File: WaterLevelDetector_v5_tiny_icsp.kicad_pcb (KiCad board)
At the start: 2 copper layers, 57 x 90 mm, 12 parts, among them J3 USB_C_Receptacle_PowerOnly_6P, J4 Conn_02x03_Odd_Even, U1 ATtiny85-20P

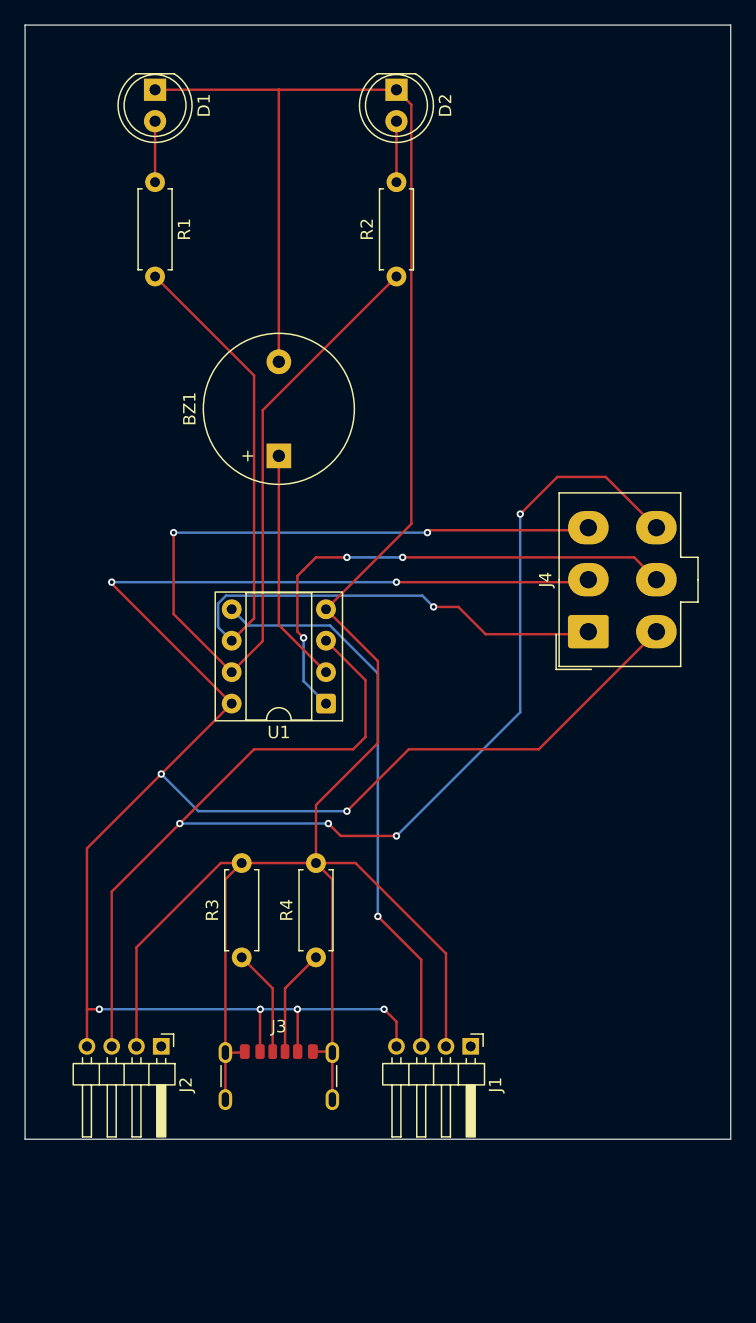
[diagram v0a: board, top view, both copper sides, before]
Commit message: made the pcb area smaller
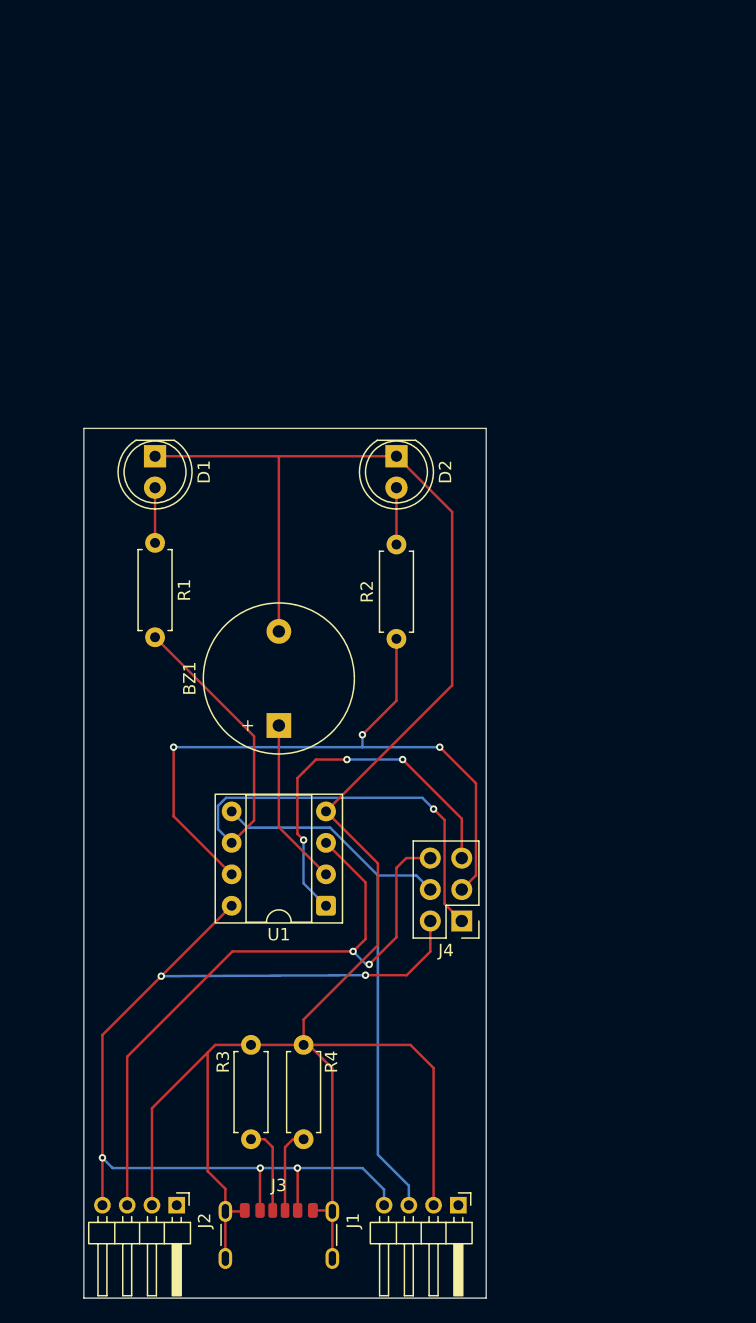
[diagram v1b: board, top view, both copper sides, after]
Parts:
- J4: footprint Connector_Molex:Molex_Mini-Fit_Jr_5566-06A_2x03_P4.20mm_Vertical -> Connector_PinHeader_2.54mm:PinHeader_2x03_P2.54mm_Vertical
- moved D1 29.6 mm to (136.0, 71.3)
- moved D2 29.6 mm to (155.5, 71.3)
- moved R2 29.3 mm to (155.5, 86.1)
- moved R1 29.1 mm to (136.0, 78.3)
- moved J4 25.5 mm to (160.8, 108.9), turned to 180 degrees
- moved BZ1 21.8 mm to (146.0, 93.1)
- moved U1 16.3 mm to (149.8, 107.6)
- moved R4 14.7 mm to (148.0, 126.5)
- moved R3 14.7 mm to (143.8, 126.5)
- moved J2 12.9 mm to (137.8, 131.8)
- moved J1 12.9 mm to (160.5, 131.8)
- moved J3 12.8 mm to (146.0, 135.3)
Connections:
- J4 pad 4: Net-(J1-Pin_4) -> Net-(J1-Pin_3)
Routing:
- net Net-(J1-Pin_4): track 166.5 -> 85.4 mm, vias 8 -> 5
- net Net-(J2-Pin_3): track 109.3 -> 57.9 mm, vias 4 -> 2
- net Net-(J4-Pin_3): track 84.4 -> 56.8 mm, vias 2 -> 3
- net Net-(BZ1--): track 200.0 -> 176.0 mm
- net Net-(J4-Pin_1): track 68.5 -> 52.2 mm
- net Net-(J4-Pin_5): track 41.6 -> 30.3 mm
- net Net-(BZ1-+): track 19.0 -> 13.6 mm
- net Net-(J3-CC2): track 8.65 -> 6.88 mm
- net Net-(J3-CC1): track 8.65 -> 7.13 mm
- net Net-(J1-Pin_3): track 45.5 -> 46.3 mm, vias 1 -> 0
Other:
- board size 57 x 90 mm -> 32.5 x 70.3 mm

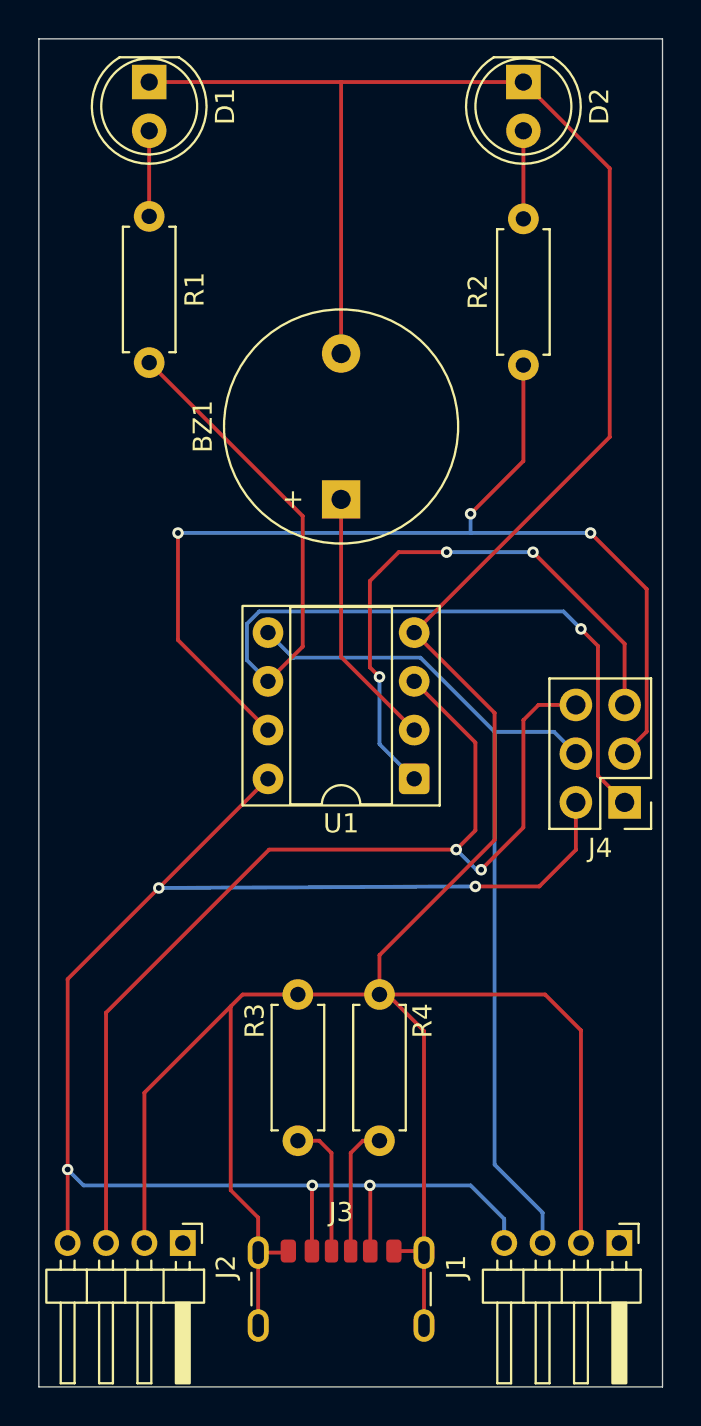
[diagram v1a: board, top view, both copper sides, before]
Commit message: made the pcb even more smaller
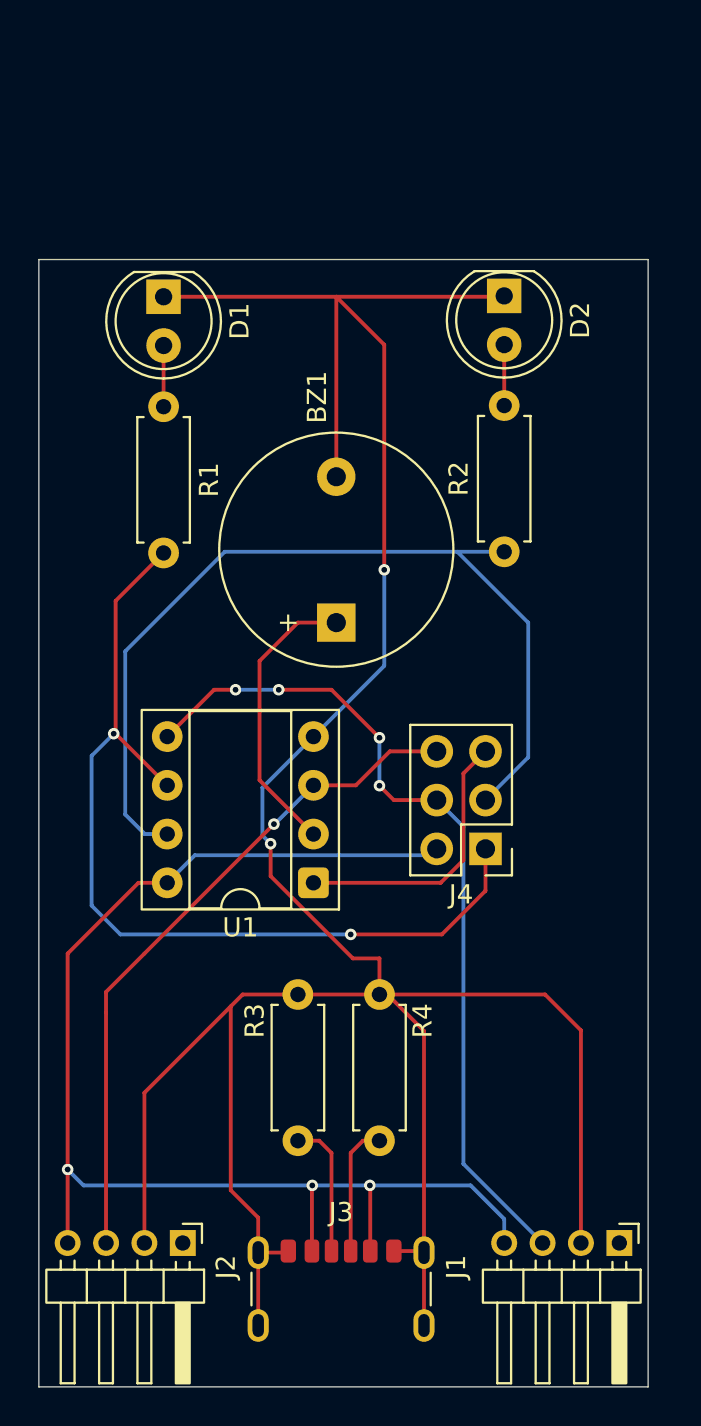
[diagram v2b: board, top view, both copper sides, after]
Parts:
- moved D1 11.2 mm to (136.8, 82.5)
- moved D2 11.2 mm to (154.5, 82.5)
- moved R1 9.95 mm to (136.8, 88.2)
- moved R2 9.78 mm to (154.5, 95.8)
- moved J4 7.64 mm to (153.5, 111.3)
- moved U1 7.55 mm to (144.6, 113.1)
- moved BZ1 6.42 mm to (145.8, 99.5)
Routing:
- net Net-(J2-Pin_3): track 57.9 -> 35.5 mm, vias 2 -> 1
- net Net-(BZ1--): track 176.0 -> 155.3 mm, vias 0 -> 2
- net Net-(J1-Pin_4): track 85.4 -> 68.5 mm, vias 5 -> 3
- net Net-(J4-Pin_5): track 30.3 -> 14.4 mm, vias 3 -> 0
- net Net-(J4-Pin_3): track 56.8 -> 48.4 mm, vias 3 -> 0
- net Net-(J4-Pin_1): track 52.2 -> 48.0 mm, vias 1 -> 2
- net Net-(J1-Pin_3): track 46.3 -> 44.3 mm, vias 0 -> 4
- net Net-(D2-A): track 4.59 -> 3.17 mm
- net Net-(BZ1-+): track 13.6 -> 15.0 mm
- net Net-(D1-A): track 4.46 -> 3.19 mm
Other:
- board size 32.5 x 70.3 mm -> 31.8 x 58.8 mm

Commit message: hopefully made the leds red and green: schematic update
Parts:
- D1: value LED -> LED_RED
- D2: value LED -> LED_GREEN
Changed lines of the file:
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@@
 			)
 		)
-		(property "Value" "LED"
+		(property "Value" "LED_RED"
 			(at 1.27 3.96 90)
 			(layer "F.Fab")
@@
 			)
 		)
-		(property "Value" "LED"
+		(property "Value" "LED_GREEN"
 			(at 1.27 3.96 90)
 			(layer "F.Fab")
